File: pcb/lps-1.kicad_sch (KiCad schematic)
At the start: 25 parts

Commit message: First layout
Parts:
- removed D?: B130-13-F, Diode_SMD:D_SMA, symbol Device:D_Schottky
- removed J?: Alt Power, Connector_PinHeader_2.54mm:PinHeader_1x02_P2.54mm_Vertical, symbol Connector:Conn_01x02_Pin
- removed J?: GPIO1, Connector_PinHeader_2.54mm:PinHeader_1x08_P2.54mm_Vertical, symbol Connector:Conn_01x08_Pin
- removed J?: GPIO2, Connector_PinHeader_2.54mm:PinHeader_1x12_P2.54mm_Vertical, symbol Connector:Conn_01x12_Pin
- removed J?: Comm, Connector_PinHeader_2.54mm:PinHeader_1x08_P2.54mm_Vertical, symbol Connector:Conn_01x08_Pin
- removed J?: Power OUT, Connector_PinHeader_2.54mm:PinHeader_1x02_P2.54mm_Vertical, symbol Connector:Conn_01x02_Pin
- removed J?: USART-USB, Connector_PinSocket_2.54mm:PinSocket_1x06_P2.54mm_Vertical, symbol Connector:Conn_01x06_Socket
- removed JP?: USB Pwr, Connector_PinHeader_2.54mm:PinHeader_1x02_P2.54mm_Vertical, symbol Jumper:SolderJumper_2_Open
- removed TC?: ISP, TagConnect:Tag-Connect EC06, symbol atmega1608_dev:Tag-Connect_EC-06
- added J1: Conn_01x12_Pin, Connector_PinHeader_1.27mm:PinHeader_1x12_P1.27mm_Vertical, symbol Connector:Conn_01x12_Pin
- added J15: PWR, Connector_PinHeader_2.54mm:PinHeader_1x06_P2.54mm_Vertical, symbol Connector_Generic:Conn_01x06
- added J2: Conn_01x06_Pin, Connector_PinHeader_1.27mm:PinHeader_1x06_P1.27mm_Vertical, symbol Connector:Conn_01x06_Pin
- added J4: A_INA219, lps-1-Footprints:Adafruit-INA219, symbol Connector_Generic:Conn_01x06
- added J5: XBEE, Connector_PinHeader_2.54mm:PinHeader_2x03_P2.54mm_Vertical, symbol Connector_Generic:Conn_01x06
- added J6: DEV, Connector_PinHeader_2.54mm:PinHeader_2x04_P2.54mm_Vertical, symbol Connector_Generic:Conn_01x08
- added Lg1: logo, sjm-mechanical:MyBasic_rounded_50_1, symbol sjm-mechanical:logo
- added TC1: ISP, TagConnect:PRG_TC2030-IDC-FP_TH, symbol Connector:Conn_01x06_Socket
- gave numbers to parts that had none: 16
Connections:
- net PF2 is gone; now on net SDA: U2.22 (PF2/TWI/AIN12/XCK2/VOUTF/2-IN2)
- net PF3 is gone; now on net SCL: U2.23 (PF3/TWI/AIN13/XDIR2/3-OUT)
- net +3.3V: now also J15.5 (Pin_5), J4.1 (Pin_1), J5.1 (Pin_1), J6.1 (Pin_1), TC1.2 (Pin_2)
- net +5V: now also J15.3 (Pin_3)
- net DIN: now also J6.5 (Pin_5)
- net DOUT: now also J6.7 (Pin_7)
- net GND: now also J15.2 (Pin_2), J15.4 (Pin_4), J15.6 (Pin_6), J4.2 (Pin_2), J5.2 (Pin_2), J6.2 (Pin_2), J6.4 (Pin_4), J6.6 (Pin_6), J6.8 (Pin_8), TC1.6 (Pin_6)
- net MISO: now also J1.4 (Pin_4)
- net MOSI: now also J1.5 (Pin_5)
- net PC2: now also J1.1 (Pin_1)
- net PC3: now also J2.1 (Pin_1)
- net PD2: now also J2.2 (Pin_2)
- net PD3: now also J2.3 (Pin_3)
- net PD4: now also J2.4 (Pin_4)
- net PD5: now also J2.5 (Pin_5)
- net PD6: now also J2.6 (Pin_6)
- net PD7: now also J1.12 (Pin_12)
- net PF0: now also J1.11 (Pin_11)
- net PF1: now also J1.10 (Pin_10)
- net PF4: now also J1.9 (Pin_9)
- net PF5: now also J1.8 (Pin_8)
- net RxD0: now also J5.4 (Pin_4)
- net SCK: now also J1.3 (Pin_3)
- net SCL: now also J4.3 (Pin_3); no longer U2.1 (PA3/TWI/XDIR0/SCL/0-WO3/1-WO/0-OUT)
- net SDA: now also J4.4 (Pin_4); no longer U2.32 (PA2/TWI/XCK0/SDA/0-WO/EVOUTA/0-IN2)
- net SS: now also J1.2 (Pin_2)
- net TxD0: now also J5.3 (Pin_3)
- net UPDI: now also J6.3 (Pin_3), TC1.1 (Pin_1)
- net 5VIN: now reaches D1.2 (A)
- net 5VIN: now also J15.1 (Pin_1)
- net PD0 renamed MODEM_RESET
- net MODEM_RESET: now also J5.6 (Pin_6)
- net PD1 renamed MODEM_SLEEP
- net MODEM_SLEEP: now also J5.5 (Pin_5)
- new net PA2: J1.7 (Pin_7), U2.32 (PA2/TWI/XCK0/SDA/0-WO/EVOUTA/0-IN2)
- new net PA3: J1.6 (Pin_6), U2.1 (PA3/TWI/XDIR0/SCL/0-WO3/1-WO/0-OUT)
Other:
- note added: "3V3 GND DIN DOUT SLEEP RESET"
- moved on the sheet: C1, C2, C3, D1, D2, H3, H4, JP1, R1, R2, R3, R4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

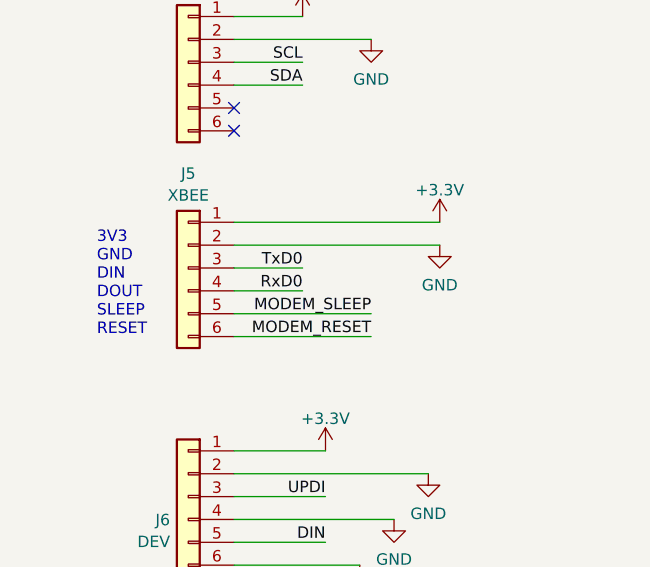
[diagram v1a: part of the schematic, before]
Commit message: Refactored the connectors for the LPS-X-1
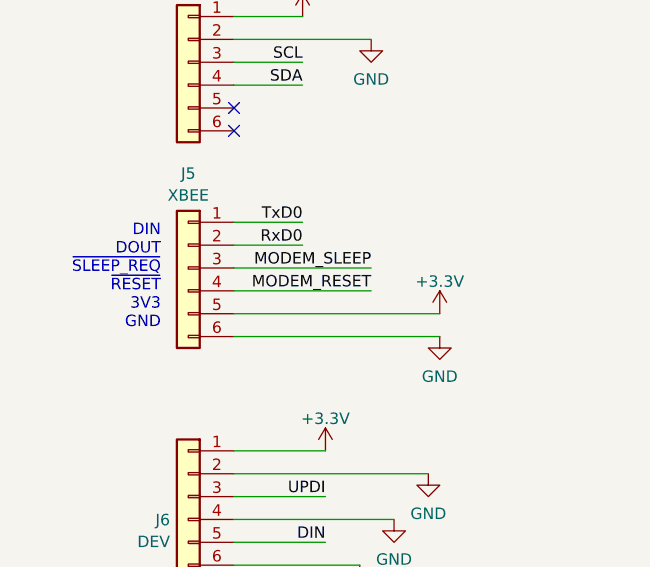
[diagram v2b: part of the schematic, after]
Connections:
- net +3.3V: now also J5.5 (Pin_5); no longer J5.1 (Pin_1)
- net GND: now also J5.6 (Pin_6); no longer J5.2 (Pin_2)
- net MODEM_RESET: now also J5.4 (Pin_4); no longer J5.6 (Pin_6)
- net MODEM_SLEEP: now also J5.3 (Pin_3); no longer J5.5 (Pin_5)
- net RxD0: now also J5.2 (Pin_2); no longer J5.4 (Pin_4)
- net TxD0: now also J5.1 (Pin_1); no longer J5.3 (Pin_3)
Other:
- note added: "DIN DOUT ~{SLEEP_REQ} ~{RESET} 3V3 GND"
- note removed: "3V3 GND DIN DOUT SLEEP RESET"

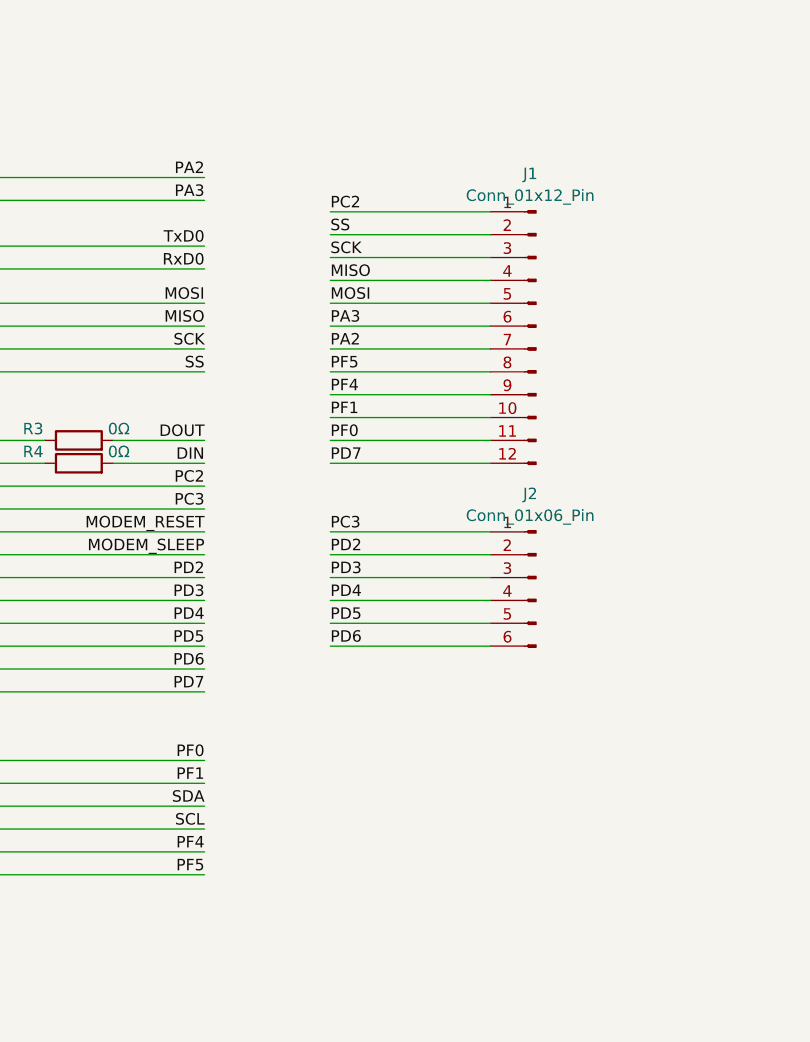
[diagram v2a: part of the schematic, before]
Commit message: Reduces the board footprint and introduces copper fills on F and B
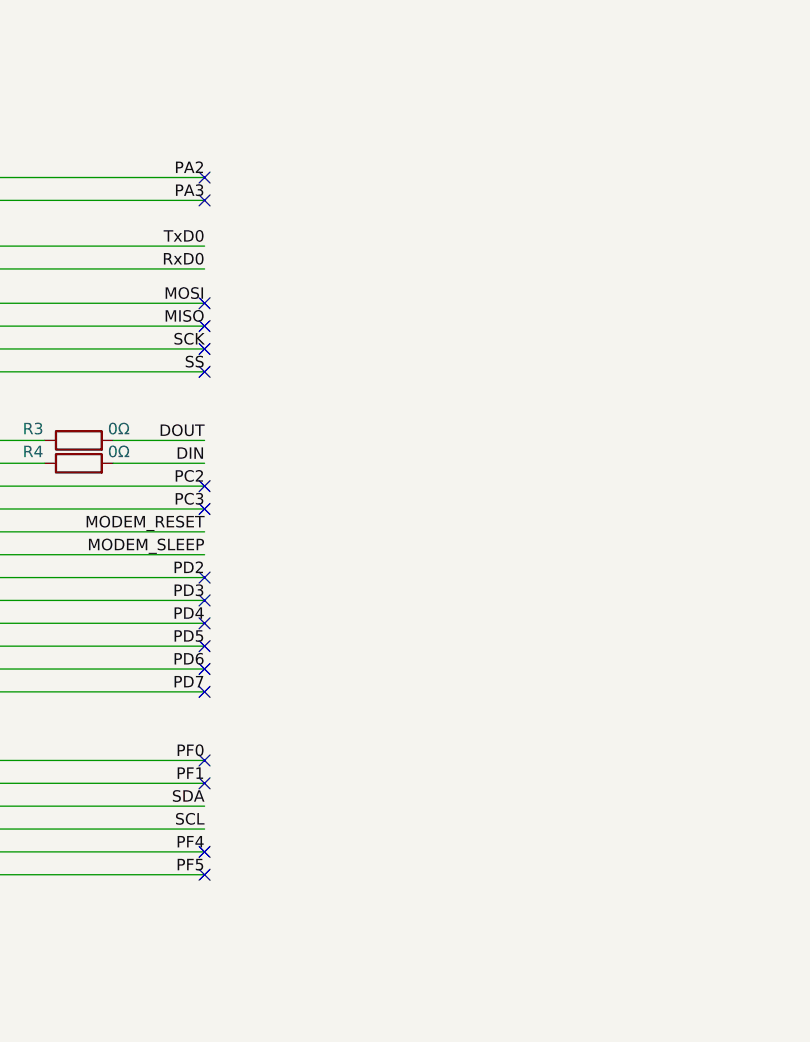
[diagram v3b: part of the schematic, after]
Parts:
- removed J1: Conn_01x12_Pin, Connector_PinHeader_1.27mm:PinHeader_1x12_P1.27mm_Vertical, symbol Connector:Conn_01x12_Pin
- removed J2: Conn_01x06_Pin, Connector_PinHeader_1.27mm:PinHeader_1x06_P1.27mm_Vertical, symbol Connector:Conn_01x06_Pin
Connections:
- no-connect marks 5 -> 23

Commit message: Rework to include a 5V LDO
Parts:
- added C1: 220μF, Capacitor_THT:CP_Radial_D10.0mm_P2.50mm, symbol Device:C_Polarized
- added C4, C5: 0.1μF, Capacitor_SMD:C_0805_2012Metric_Pad1.18x1.45mm_HandSolder, symbol Device:C
- added C6: 10μF, Capacitor_THT:CP_Radial_D5.0mm_P2.50mm, symbol Device:C_Polarized
- added HS1: Heatsink, lps-1-Footprints:Wakefield-E274_13.1x19.3mm, symbol Mechanical:Heatsink
- added U1: L7805, Package_TO_SOT_THT:TO-220-3_Vertical, symbol Regulator_Linear:L7805
- renumbered C1 to C7, U1 to U3
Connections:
- net +5V: now also C5.1, C6.1, U1.3 (OUT); no longer D1.1 (K)
- net GND: now also C1.2, C4.2, C5.2, C6.2, U1.2 (GND)
- net 5VIN renamed 12VIN
- new net: C1.1, C4.1, D1.1 (K), U1.1 (IN)
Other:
- moved on the sheet: C2, C3, C7, D2, H3, H4, J15, J4, J5, J6, JP1, R1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

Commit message: Reworked the connectors
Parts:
- removed HS1: Heatsink, lps-1-Footprints:Wakefield-E274_13.1x19.3mm, symbol Mechanical:Heatsink
- removed TC1: ISP, TagConnect:PRG_TC2030-IDC-FP_TH, symbol Connector:Conn_01x06_Socket
- J6: footprint Connector_PinHeader_2.54mm:PinHeader_2x04_P2.54mm_Vertical -> Connector_PinHeader_2.54mm:PinHeader_1x08_P2.54mm_Vertical
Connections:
- no-connect marks 23 -> 20

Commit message: Revision 1.0
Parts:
- J4: footprint lps-1-Footprints:Adafruit-INA219 -> lps-1-Footprints:Adafruit-INA219_2xM2.5
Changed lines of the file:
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@@
 	)
 	(junction
-		(at 35.56 50.8)
+		(at 66.04 50.8)
 		(diameter 0)
 		(color 0 0 0 0)
@@
 	(wire
 		(pts
-			(xy 35.56 50.8) (xy 41.91 50.8)
-		)
-		(stroke
-			(width 0)
-			(type default)
-		)
-	)
-	(wire
-		(pts
-			(xy 24.13 50.8) (xy 35.56 50.8)
+			(xy 24.13 50.8) (xy 41.91 50.8)
 		)
 		(stroke
@@
 	(wire
 		(pts
+			(xy 66.04 50.8) (xy 71.12 50.8)
+		)
+		(stroke
+			(width 0)
+			(type default)
+		)
+	)
+	(wire
+		(pts
 			(xy 222.25 104.14) (xy 222.25 109.22)
 		)
@@
 	(wire
 		(pts
-			(xy 35.56 45.72) (xy 35.56 50.8)
+			(xy 66.04 45.72) (xy 66.04 50.8)
 		)
 		(stroke
@@
 	(wire
 		(pts
-			(xy 57.15 50.8) (xy 71.12 50.8)
+			(xy 57.15 50.8) (xy 66.04 50.8)
 		)
 		(stroke
@@
 			)
 		)
-		(property "Description" ""
+		(property "Description" "Power symbol creates a global label with name \"GND\" , ground"
 			(at 236.22 236.22 0)
 			(effects
@@
 			)
 		)
-		(property "Footprint" "lps-1-Footprints:Adafruit-INA219"
+		(property "Footprint" "lps-1-Footprints:Adafruit-INA219_2xM2.5"
 			(at 81.28 160.02 0)
 			(effects
@@
 			)
 		)
-		(property "Description" ""
+		(property "Description" "Special symbol for telling ERC where power comes from"
 			(at 142.24 63.5 0)
 			(effects
@@
 			)
 		)
-		(property "Description" ""
+		(property "Description" "Power symbol creates a global label with name \"GND\" , ground"
 			(at 96.52 220.98 0)
 			(effects
@@
 			)
 		)
-		(property "Description" ""
+		(property "Description" "Power symbol creates a global label with name \"GND\" , ground"
 			(at 168.91 83.82 0)
 			(effects
@@
 			)
 		)
-		(property "Description" ""
+		(property "Description" "Power symbol creates a global label with name \"GND\" , ground"
 			(at 101.6 157.48 0)
 			(effects
@@
 	(symbol
 		(lib_id "power:PWR_FLAG")
-		(at 35.56 45.72 0)
+		(at 66.04 45.72 0)
 		(unit 1)
 		(exclude_from_sim no)
@@
 		(fields_autoplaced yes)
 		(property "Reference" "#FLG0102"
-			(at 35.56 43.815 0)
+			(at 66.04 43.815 0)
 			(effects
 				(font
@@
 		)
 		(property "Value" "PWR_FLAG"
-			(at 35.56 42.1442 0)
+			(at 66.04 42.1442 0)
 			(effects
 				(font
@@
 		)
 		(property "Footprint" ""
-			(at 35.56 45.72 0)
+			(at 66.04 45.72 0)
 			(effects
 				(font
@@
 		)
 		(property "Datasheet" "~"
-			(at 35.56 45.72 0)
+			(at 66.04 45.72 0)
 			(effects
 				(font
@@
 			)
 		)
-		(property "Description" ""
-			(at 35.56 45.72 0)
+		(property "Description" "Special symbol for telling ERC where power comes from"
+			(at 66.04 45.72 0)
 			(effects
 				(font
@@
 			)
 		)
-		(property "Description" ""
+		(property "Description" "Power symbol creates a global label with name \"GND\" , ground"
 			(at 109.22 190.5 0)
 			(effects
@@
 			)
 		)
-		(property "Description" ""
+		(property "Description" "Power symbol creates a global label with name \"+5V\""
 			(at 97.79 129.54 0)
 			(effects
@@
 			)
 		)
-		(property "Description" ""
+		(property "Description" "Power symbol creates a global label with name \"GND\" , ground"
 			(at 189.23 158.75 0)
 			(effects
@@
 			)
 		)
-		(property "Description" ""
+		(property "Description" "Power symbol creates a global label with name \"+3.3V\""
 			(at 172.72 48.26 0)
 			(effects
@@
 			)
 		)
-		(property "Description" ""
+		(property "Description" "Power symbol creates a global label with name \"GND\" , ground"
 			(at 227.33 121.92 0)
 			(effects
@@
 			)
 		)
-		(property "Description" ""
+		(property "Description" "Power symbol creates a global label with name \"GND\" , ground"
 			(at 92.71 140.97 0)
 			(effects
@@
 			)
 		)
-		(property "Description" ""
+		(property "Description" "Power symbol creates a global label with name \"+5V\""
 			(at 121.92 46.99 0)
 			(effects
@@
 			)
 		)
-		(property "Description" ""
+		(property "Description" "Power symbol creates a global label with name \"GND\" , ground"
 			(at 100.33 215.9 0)
 			(effects
@@
 			)
 		)
-		(property "Description" ""
+		(property "Description" "Power symbol creates a global label with name \"GND\" , ground"
 			(at 148.59 63.5 0)
 			(effects
@@
 			)
 		)
-		(property "Description" ""
+		(property "Description" "Power symbol creates a global label with name \"+3.3V\""
 			(at 222.25 104.14 0)
 			(effects
@@
 			)
 		)
-		(property "Description" ""
+		(property "Description" "Power symbol creates a global label with name \"+3.3V\""
 			(at 109.22 187.96 0)
 			(effects
@@
 			)
 		)
-		(property "Description" ""
+		(property "Description" "Power symbol creates a global label with name \"+3.3V\""
 			(at 96.52 203.2 0)
 			(effects
@@
 			)
 		)
-		(property "Description" ""
+		(property "Description" "Power symbol creates a global label with name \"GND\" , ground"
 			(at 107.95 205.74 0)
 			(effects
@@
 			)
 		)
-		(property "Description" ""
+		(property "Description" "Power symbol creates a global label with name \"+3.3V\""
 			(at 93.98 154.94 0)
 			(effects
@@
 			)
 		)
-		(property "Description" ""
+		(property "Description" "Power symbol creates a global label with name \"GND\" , ground"
 			(at 83.82 67.31 0)
 			(effects
@@
 			)
 		)
-		(property "Description" ""
+		(property "Description" "Power symbol creates a global label with name \"GND\" , ground"
 			(at 104.14 210.82 0)
 			(effects
@@
 			)
 		)
-		(property "Description" ""
+		(property "Description" "Power symbol creates a global label with name \"+3.3V\""
 			(at 101.6 134.62 0)
 			(effects

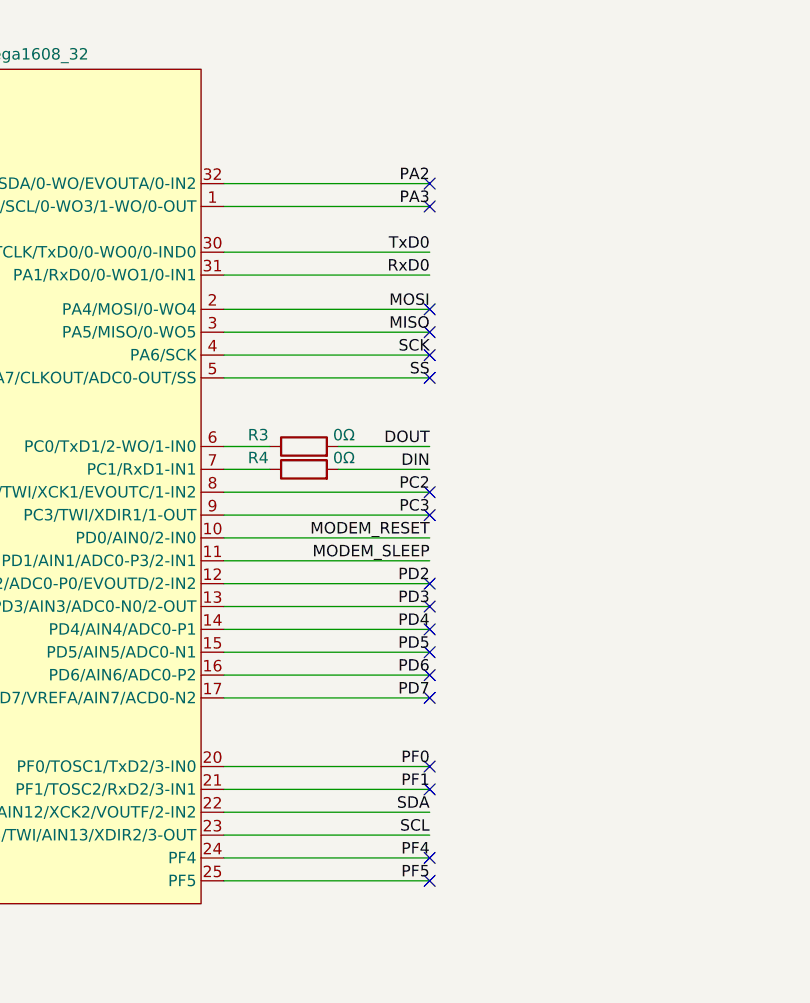
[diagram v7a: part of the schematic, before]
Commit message: Correction to the TWI0 pin selection
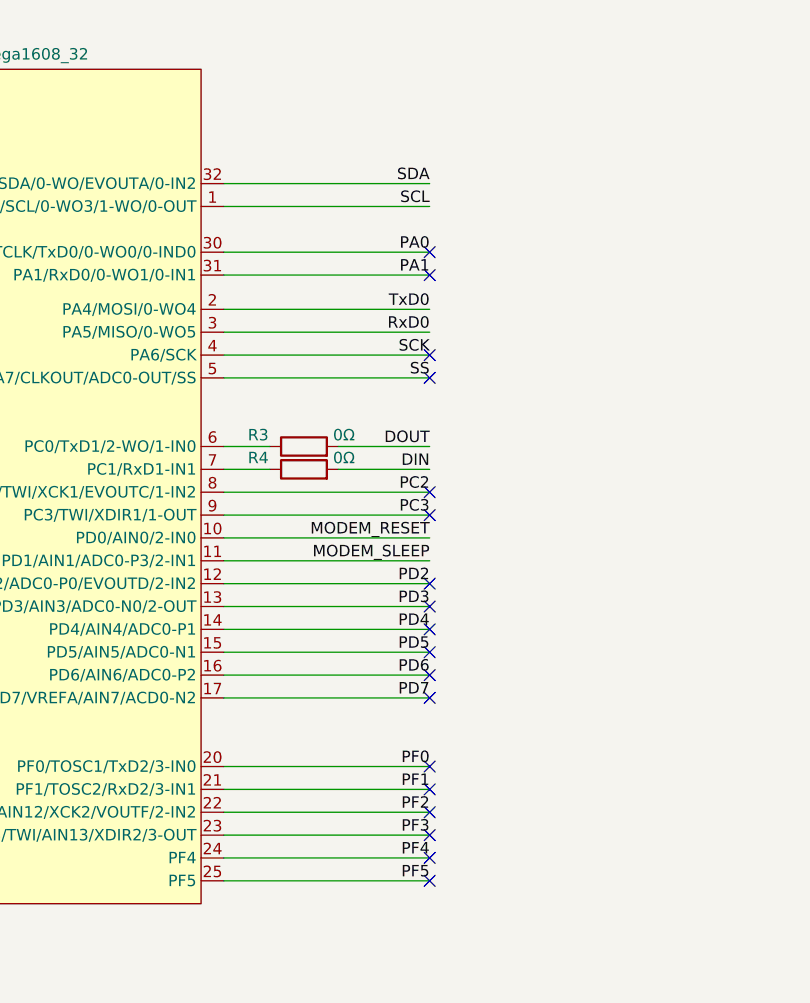
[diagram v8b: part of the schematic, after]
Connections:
- net MISO is gone; now on net RxD0: U2.3 (PA5/MISO/0-WO5)
- net MOSI is gone; now on net TxD0: U2.2 (PA4/MOSI/0-WO4)
- net PA2 is gone; now on net SDA: U2.32 (PA2/TWI/XCK0/SDA/0-WO/EVOUTA/0-IN2)
- net PA3 is gone; now on net SCL: U2.1 (PA3/TWI/XDIR0/SCL/0-WO3/1-WO/0-OUT)
- net RxD0: no longer U2.31 (PA1/RxD0/0-WO1/0-IN1)
- net SCL: no longer U2.23 (PF3/TWI/AIN13/XDIR2/3-OUT)
- net SDA: no longer U2.22 (PF2/TWI/AIN12/XCK2/VOUTF/2-IN2)
- net TxD0: no longer U2.30 (PA0/EXTCLK/TxD0/0-WO0/0-IND0)
- new net PA0: U2.30 (PA0/EXTCLK/TxD0/0-WO0/0-IND0)
- new net PA1: U2.31 (PA1/RxD0/0-WO1/0-IN1)
- new net PF2: U2.22 (PF2/TWI/AIN12/XCK2/VOUTF/2-IN2)
- new net PF3: U2.23 (PF3/TWI/AIN13/XDIR2/3-OUT)
